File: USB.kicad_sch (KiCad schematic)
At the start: 10 parts, among them U401 ASDMB-26.000MHz-C, U402 USB3343

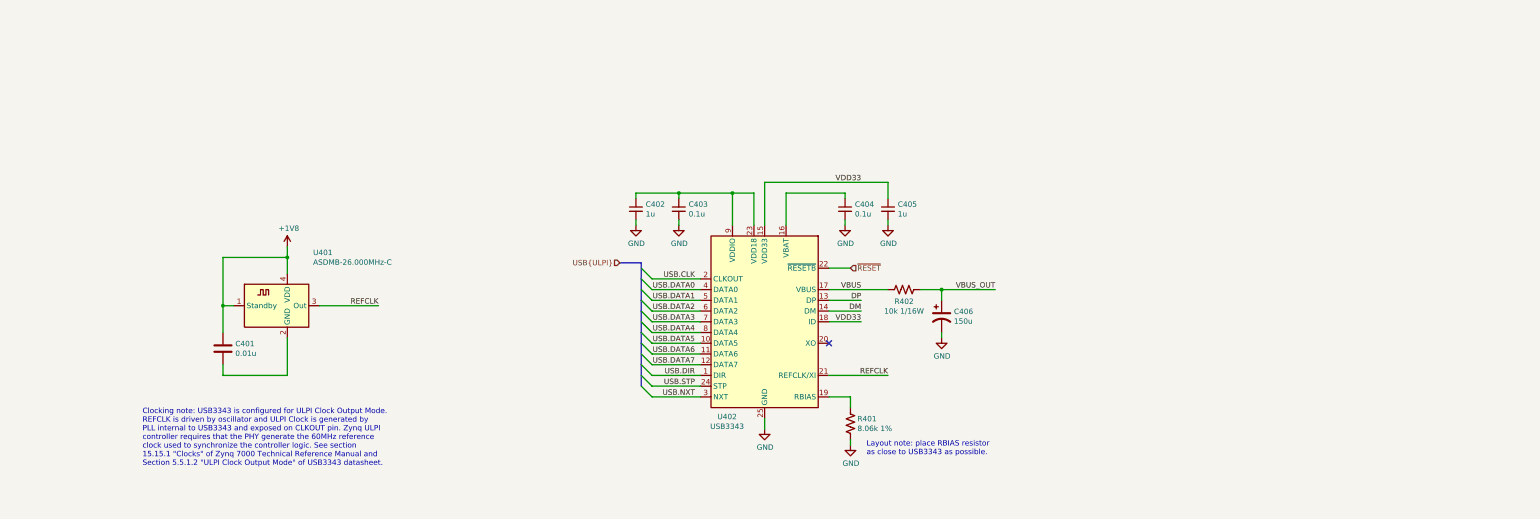
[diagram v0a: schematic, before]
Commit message: Fix footprint associations, use 74LVC2G07 instead of MOSFETs
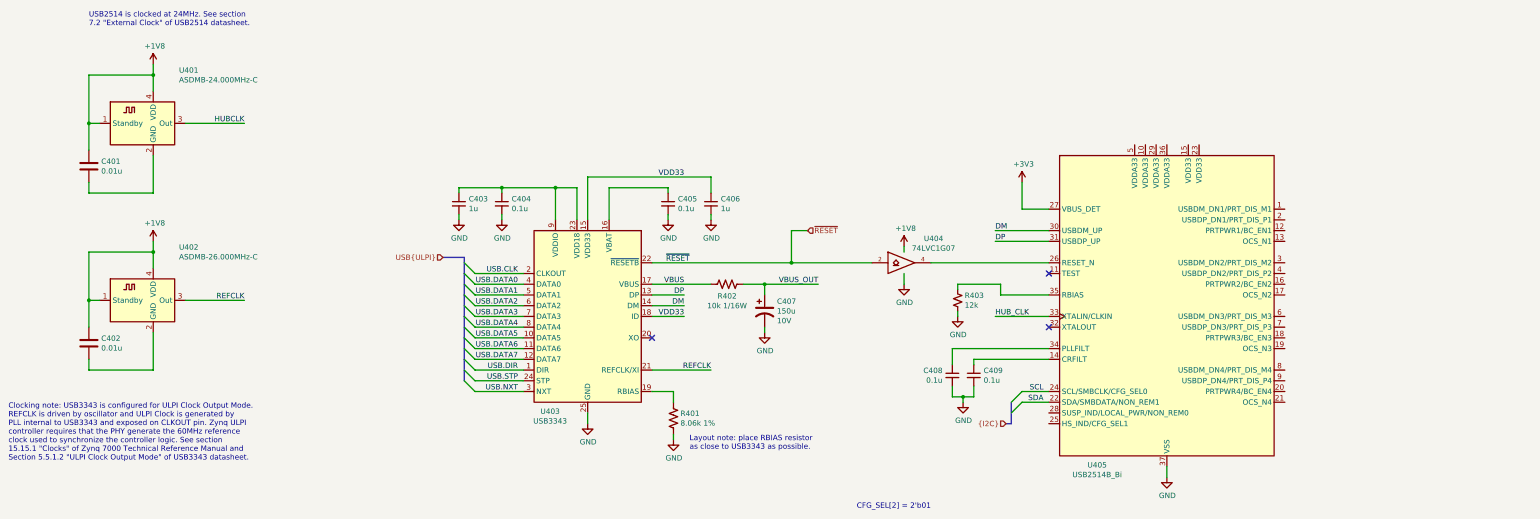
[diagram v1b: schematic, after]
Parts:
- added C401: 0.01u, Capacitor_SMD:C_0402_1005Metric, symbol Device:C
- added C408, C409: 0.1u, Capacitor_SMD:C_0402_1005Metric, symbol Device:C_Small
- added R403: 12k, Resistor_SMD:R_0402_1005Metric, symbol Device:R_Small_US
- added U401: ASDMB-24.000MHz-C, Oscillator:Oscillator_SMD_Abracon_ASDMB-4Pin_2.5x2.0mm, symbol Oscillator:ASDMB-xxxMHz
- added U404: 74LVC1G07, Package_TO_SOT_SMD:SOT-553, symbol 74xGxx:74LVC1G07
- added U405: USB2514B_Bi, Package_DFN_QFN:QFN-36-1EP_6x6mm_P0.5mm_EP3.7x3.7mm, symbol Interface_USB:USB2514B_Bi
- C402: renamed from C401; footprint (none) -> Capacitor_SMD:C_0402_1005Metric
- C403: renamed from C402; footprint (none) -> Capacitor_SMD:C_0402_1005Metric
- C404: renamed from C403; footprint (none) -> Capacitor_SMD:C_0402_1005Metric
- C405: renamed from C404; footprint (none) -> Capacitor_SMD:C_0402_1005Metric
- C406: renamed from C405; footprint (none) -> Capacitor_SMD:C_0402_1005Metric
- C407: renamed from C406; footprint (none) -> Capacitor_SMD:CP_Elec_3x5.3; Voltage (none) -> 10V
- R401, R402: footprint (none) -> Resistor_SMD:R_0402_1005Metric
- renumbered U401 to U402, U402 to U403
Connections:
- net +1V8: now also C401.1, U401.1 (Standby), U401.4 (VDD), U404.5 (VCC)
- net DM: now also U405.30 (USBDM_UP)
- net DP: now also U405.31 (USBDP_UP)
- net GND: now also C408.2, C409.2, R403.2, U404.3 (GND), U405.37 (VSS)
- net ~RESET: now also U404.2
- new net: C408.1, U405.34 (PLLFILT)
- new net: C409.1, U405.14 (CRFILT)
- new net: U404.4, U405.26 (RESET_N)
- new net: R403.1, U405.35 (RBIAS)
- new net: C401.2, U401.2 (GND)
- new net +3V3: U405.27 (VBUS_DET)
- new net HUBCLK: U401.3 (Out)
- new net HUB_CLK: U405.33 (XTALIN/CLKIN)
- new net SCL: U405.24 (SCL/SMBCLK/CFG_SEL0)
- new net SDA: U405.22 (SDA/SMBDATA/NON_REM1)
- no-connect marks 1 -> 3
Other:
- note added: "CFG_SEL[2] = 2'b01"
- note added: "USB2514 is clocked at 24MHz. See section 7.2 "External Clock" of USB2514 datasheet."
- moved on the sheet: C402, C403, C404, C405, C406, C407, R401, R402, U402, U403

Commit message: Connect Ethernet and USB to MIO, start layout
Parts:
- added J401, J402: USB_A, Connector_USB:USB_A_Molex_67643_Horizontal, symbol Connector:USB_A
- C401, C402, C403, C404, C405, C406, C408, C409: footprint Capacitor_SMD:C_0402_1005Metric -> Capacitor_SMD:C_0603_1608Metric
- R401, R402, R403: footprint Resistor_SMD:R_0402_1005Metric -> Resistor_SMD:R_0603_1608Metric
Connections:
- net D1P: now reaches U405.1 (USBDM_DN1/PRT_DIS_M1)
- net D1P: now also J401.3 (D+)
- net D1N: now reaches U405.2 (USBDP_DN1/PRT_DIS_P1)
- net D1N: now also J401.2 (D-)
- net D2P: now reaches U405.3 (USBDM_DN2/PRT_DIS_M2)
- net D2P: now also J402.3 (D+)
- net D2N: now reaches U405.4 (USBDP_DN2/PRT_DIS_P2)
- net D2N: now also J402.2 (D-)
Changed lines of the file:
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@@
   (junction (at 212.09 116.84) (diameter 0) (color 0 0 0 0))
   (junction (at 252.73 148.59) (diameter 0) (color 0 0 0 0))
+  (no_connect (at 273.05 119.38))
+  (no_connect (at 179.07 134.62))
   (no_connect (at 273.05 132.08))
-  (no_connect (at 179.07 134.62))
-  (no_connect (at 273.05 119.38))
   (bus_entry (at 134.62 116.84) (size 2.54 2.54)
     (stroke (width 0.1524) (type solid) (color 0 0 0 0))
@@
   )
   (wire (pts (xy 300.99 165.1) (xy 300.99 167.64))
+    (stroke (width 0) (type solid) (color 0 0 0 0))
+  )
+  (wire (pts (xy 328.93 104.14) (xy 341.63 104.14))
+    (stroke (width 0) (type solid) (color 0 0 0 0))
+  )
+  (wire (pts (xy 328.93 106.68) (xy 341.63 106.68))
+    (stroke (width 0) (type solid) (color 0 0 0 0))
+  )
+  (wire (pts (xy 328.93 116.84) (xy 341.63 116.84))
+    (stroke (width 0) (type solid) (color 0 0 0 0))
+  )
+  (wire (pts (xy 328.93 119.38) (xy 341.63 119.38))
+    (stroke (width 0) (type solid) (color 0 0 0 0))
+  )
+  (wire (pts (xy 377.19 88.9) (xy 386.08 88.9))
+    (stroke (width 0) (type solid) (color 0 0 0 0))
+  )
+  (wire (pts (xy 377.19 91.44) (xy 386.08 91.44))
+    (stroke (width 0) (type solid) (color 0 0 0 0))
+  )
+  (wire (pts (xy 378.46 129.54) (xy 387.35 129.54))
+    (stroke (width 0) (type solid) (color 0 0 0 0))
+  )
+  (wire (pts (xy 378.46 132.08) (xy 387.35 132.08))
     (stroke (width 0) (type solid) (color 0 0 0 0))
   )
@@
     (effects (font (size 1.27 1.27)) (justify right bottom))
   )
-  (hierarchical_label "USB{ULPI}" (shape input) (at 129.54 115.57 180)
+  (label "D1P" (at 341.63 104.14 180)
+    (effects (font (size 1.27 1.27)) (justify right bottom))
+  )
+  (label "D1N" (at 341.63 106.68 180)
+    (effects (font (size 1.27 1.27)) (justify right bottom))
+  )
+  (label "D2P" (at 341.63 116.84 180)
+    (effects (font (size 1.27 1.27)) (justify right bottom))
+  )
+  (label "D2N" (at 341.63 119.38 180)
+    (effects (font (size 1.27 1.27)) (justify right bottom))
+  )
+  (label "D1P" (at 386.08 88.9 180)
+    (effects (font (size 1.27 1.27)) (justify right bottom))
+  )
+  (label "D1N" (at 386.08 91.44 180)
+    (effects (font (size 1.27 1.27)) (justify right bottom))
+  )
+  (label "D2P" (at 387.35 129.54 180)
+    (effects (font (size 1.27 1.27)) (justify right bottom))
+  )
+  (label "D2N" (at 387.35 132.08 180)
+    (effects (font (size 1.27 1.27)) (justify right bottom))
+  )
+  (hierarchical_label "USB{ULPI}" (shape bidirectional) (at 129.54 115.57 180)
     (effects (font (size 1.27 1.27)) (justify right))
   )
@@
       (effects (font (size 1.27 1.27)) (justify left))
     )
-    (property "Footprint" "Resistor_SMD:R_0402_1005Metric" (id 2) (at 251.46 125.73 0)
+    (property "Footprint" "Resistor_SMD:R_0603_1608Metric" (id 2) (at 251.46 125.73 0)
       (effects (font (size 1.27 1.27)) hide)
     )
@@
       (effects (font (size 1.27 1.27)) (justify left))
     )
-    (property "Footprint" "Resistor_SMD:R_0402_1005Metric" (id 2) (at 185.166 153.924 90)
+    (property "Footprint" "Resistor_SMD:R_0603_1608Metric" (id 2) (at 185.166 153.924 90)
       (effects (font (size 1.27 1.27)) hide)
     )
@@
     (property "Reference" "R402" (id 0) (at 196.85 124.7204 90))
     (property "Value" "10k 1/16W" (id 1) (at 196.85 127.0191 90))
-    (property "Footprint" "Resistor_SMD:R_0402_1005Metric" (id 2) (at 197.104 120.904 90)
+    (property "Footprint" "Resistor_SMD:R_0603_1608Metric" (id 2) (at 197.104 120.904 90)
       (effects (font (size 1.27 1.27)) hide)
     )
@@
       (effects (font (size 1.27 1.27)) (justify left))
     )
-    (property "Footprint" "Capacitor_SMD:C_0402_1005Metric" (id 2) (at 133.35 102.87 0)
+    (property "Footprint" "Capacitor_SMD:C_0603_1608Metric" (id 2) (at 133.35 102.87 0)
       (effects (font (size 1.27 1.27)) hide)
     )
@@
       (effects (font (size 1.27 1.27)) (justify left))
     )
-    (property "Footprint" "Capacitor_SMD:C_0402_1005Metric" (id 2) (at 143.51 102.87 0)
+    (property "Footprint" "Capacitor_SMD:C_0603_1608Metric" (id 2) (at 143.51 102.87 0)
       (effects (font (size 1.27 1.27)) hide)
     )
@@
       (effects (font (size 1.27 1.27)) (justify left))
     )
-    (property "Footprint" "Capacitor_SMD:C_0402_1005Metric" (id 2) (at 182.88 102.87 0)
+    (property "Footprint" "Capacitor_SMD:C_0603_1608Metric" (id 2) (at 182.88 102.87 0)
       (effects (font (size 1.27 1.27)) hide)
     )
@@
       (effects (font (size 1.27 1.27)) (justify left))
     )
-    (property "Footprint" "Capacitor_SMD:C_0402_1005Metric" (id 2) (at 193.04 102.87 0)
+    (property "Footprint" "Capacitor_SMD:C_0603_1608Metric" (id 2) (at 193.04 102.87 0)
       (effects (font (size 1.27 1.27)) hide)
     )
@@
       (effects (font (size 1.27 1.27)) (justify right))
     )
-    (property "Footprint" "Capacitor_SMD:C_0402_1005Metric" (id 2) (at 250.19 143.51 0)
+    (property "Footprint" "Capacitor_SMD:C_0603_1608Metric" (id 2) (at 250.19 143.51 0)
       (effects (font (size 1.27 1.27)) hide)
     )
@@
       (effects (font (size 1.27 1.27)) (justify left))
     )
-    (property "Footprint" "Capacitor_SMD:C_0402_1005Metric" (id 2) (at 255.27 143.51 0)
+    (property "Footprint" "Capacitor_SMD:C_0603_1608Metric" (id 2) (at 255.27 143.51 0)
       (effects (font (size 1.27 1.27)) hide)
     )
@@
       (effects (font (size 1.27 1.27)) (justify left))
     )
-    (property "Footprint" "Capacitor_SMD:C_0402_1005Metric" (id 2) (at 46.6852 97.79 0)
+    (property "Footprint" "Capacitor_SMD:C_0603_1608Metric" (id 2) (at 46.6852 97.79 0)
       (effects (font (size 1.27 1.27)) hide)
     )
@@
       (effects (font (size 1.27 1.27)) (justify left))
     )
-    (property "Footprint" "Capacitor_SMD:C_0402_1005Metric" (id 2) (at 46.6852 139.7 0)
+    (property "Footprint" "Capacitor_SMD:C_0603_1608Metric" (id 2) (at 46.6852 139.7 0)
       (effects (font (size 1.27 1.27)) hide)
     )
@@
       (effects (font (size 1.27 1.27)) hide)
     )
+  )
+  (symbol (lib_id "Connector:USB_A") (at 369.57 88.9 0) (unit 1)
+    (in_bom yes) (on_board yes)
+    (property "Reference" "J401" (id 0) (at 370.967 77.0698 0))
+    (property "Value" "USB_A" (id 1) (at 370.967 79.3685 0))
+    (property "Footprint" "Connector_USB:USB_A_Molex_67643_Horizontal" (id 2) (at 373.38 90.17 0)
+      (effects (font (size 1.27 1.27)) hide)
+    )
+    (property "Datasheet" " ~" (id 3) (at 373.38 90.17 0)
+      (effects (font (size 1.27 1.27)) hide)
+    )
+  )
+  (symbol (lib_id "Connector:USB_A") (at 370.84 129.54 0) (unit 1)
+    (in_bom yes) (on_board yes)
+    (property "Reference" "J402" (id 0) (at 372.237 117.7098 0))
+    (property "Value" "USB_A" (id 1) (at 372.237 120.0085 0))
+    (property "Footprint" "Connector_USB:USB_A_Molex_67643_Horizontal" (id 2) (at 374.65 130.81 0)
+      (effects (font (size 1.27 1.27)) hide)
+    )
+    (property "Datasheet" " ~" (id 3) (at 374.65 130.81 0)
+      (effects (font (size 1.27 1.27)) hide)
+    )

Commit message: Place motor drivers, start layout of Ethernet PHY
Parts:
- C401, C402, C403, C404, C405, C406, C408, C409: footprint Capacitor_SMD:C_0603_1608Metric -> Capacitor_SMD:C_0402_1005Metric
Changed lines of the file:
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@@
-(kicad_sch (version 20200618) (host eeschema "5.99.0-unknown-77313e4~101~ubuntu20.04.1")
+(kicad_sch (version 20200618) (host eeschema "5.99.0-unknown-7340c97~102~ubuntu20.04.1")
   (page 4 14)
   (paper "B")
@@
   (junction (at 212.09 116.84) (diameter 0) (color 0 0 0 0))
   (junction (at 252.73 148.59) (diameter 0) (color 0 0 0 0))
+  (no_connect (at 179.07 134.62))
   (no_connect (at 273.05 119.38))
-  (no_connect (at 179.07 134.62))
   (no_connect (at 273.05 132.08))
   (bus_entry (at 134.62 116.84) (size 2.54 2.54)
@@
       (effects (font (size 1.27 1.27)) (justify left))
     )
-    (property "Footprint" "Capacitor_SMD:C_0603_1608Metric" (id 2) (at 133.35 102.87 0)
+    (property "Footprint" "Capacitor_SMD:C_0402_1005Metric" (id 2) (at 133.35 102.87 0)
       (effects (font (size 1.27 1.27)) hide)
     )
@@
       (effects (font (size 1.27 1.27)) (justify left))
     )
-    (property "Footprint" "Capacitor_SMD:C_0603_1608Metric" (id 2) (at 143.51 102.87 0)
+    (property "Footprint" "Capacitor_SMD:C_0402_1005Metric" (id 2) (at 143.51 102.87 0)
       (effects (font (size 1.27 1.27)) hide)
     )
@@
       (effects (font (size 1.27 1.27)) (justify left))
     )
-    (property "Footprint" "Capacitor_SMD:C_0603_1608Metric" (id 2) (at 182.88 102.87 0)
+    (property "Footprint" "Capacitor_SMD:C_0402_1005Metric" (id 2) (at 182.88 102.87 0)
       (effects (font (size 1.27 1.27)) hide)
     )
@@
       (effects (font (size 1.27 1.27)) (justify left))
     )
-    (property "Footprint" "Capacitor_SMD:C_0603_1608Metric" (id 2) (at 193.04 102.87 0)
+    (property "Footprint" "Capacitor_SMD:C_0402_1005Metric" (id 2) (at 193.04 102.87 0)
       (effects (font (size 1.27 1.27)) hide)
     )
@@
       (effects (font (size 1.27 1.27)) (justify right))
     )
-    (property "Footprint" "Capacitor_SMD:C_0603_1608Metric" (id 2) (at 250.19 143.51 0)
+    (property "Footprint" "Capacitor_SMD:C_0402_1005Metric" (id 2) (at 250.19 143.51 0)
       (effects (font (size 1.27 1.27)) hide)
     )
@@
       (effects (font (size 1.27 1.27)) (justify left))
     )
-    (property "Footprint" "Capacitor_SMD:C_0603_1608Metric" (id 2) (at 255.27 143.51 0)
+    (property "Footprint" "Capacitor_SMD:C_0402_1005Metric" (id 2) (at 255.27 143.51 0)
       (effects (font (size 1.27 1.27)) hide)
     )
@@
       (effects (font (size 1.27 1.27)) (justify left))
     )
-    (property "Footprint" "Capacitor_SMD:C_0603_1608Metric" (id 2) (at 46.6852 97.79 0)
+    (property "Footprint" "Capacitor_SMD:C_0402_1005Metric" (id 2) (at 46.6852 97.79 0)
       (effects (font (size 1.27 1.27)) hide)
     )
@@
       (effects (font (size 1.27 1.27)) (justify left))
     )
-    (property "Footprint" "Capacitor_SMD:C_0603_1608Metric" (id 2) (at 46.6852 139.7 0)
-      (effects (font (size 1.27 1.27)) hide)
-    )
+    (property "Footprint" "Capacitor_SMD:C_0402_1005Metric" (id 2) (at 46.6852 139.7 0)
+      (effects (font (size 1.27 1.27)) hide)
+    )

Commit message: Add FTDI chip
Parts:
- renumbered C401 to C501, C402 to C502, C403 to C503, C404 to C504, C405 to C505, C406 to C506, C407 to C507, C408 to C508, C409 to C509, J401 to J501, J402 to J502, R401 to R501, R402 to R502, R403 to R503, U401 to U501, U402 to U502, U403 to U503, U404 to U504, U405 to U505

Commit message: Attach ethernet to PL, layout and route
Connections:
- net ~HUB_RESET: now reaches U504.4, U505.26 (RESET_N)
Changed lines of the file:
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@@
-(kicad_sch (version 20200714) (host eeschema "5.99.0-unknown-bf445c1~102~ubuntu20.04.1")
-  (page 1 15)
+(kicad_sch (version 20200714) (host eeschema "5.99.0-unknown-a146cd9~102~ubuntu20.04.1")
+  (page 5 15)
   (paper "B")
   (title_block
@@
   )
   (bus_alias "ULPI" (members "DATA[7..0]" "CLK" "STP" "DIR" "NXT"))
-  (junction (at 45.72 83.82) (diameter 0) (color 0 0 0 0))
-  (junction (at 45.72 125.73) (diameter 0) (color 0 0 0 0))
-  (junction (at 60.96 72.39) (diameter 0) (color 0 0 0 0))
-  (junction (at 60.96 114.3) (diameter 0) (color 0 0 0 0))
-  (junction (at 143.51 99.06) (diameter 0) (color 0 0 0 0))
-  (junction (at 156.21 99.06) (diameter 0) (color 0 0 0 0))
-  (junction (at 205.74 121.92) (diameter 0) (color 0 0 0 0))
-  (junction (at 212.09 116.84) (diameter 0) (color 0 0 0 0))
-  (junction (at 252.73 148.59) (diameter 0) (color 0 0 0 0))
-  (no_connect (at 273.05 132.08))
+  (junction (at 45.72 83.82) (diameter 1.016) (color 0 0 0 0))
+  (junction (at 45.72 125.73) (diameter 1.016) (color 0 0 0 0))
+  (junction (at 60.96 72.39) (diameter 1.016) (color 0 0 0 0))
+  (junction (at 60.96 114.3) (diameter 1.016) (color 0 0 0 0))
+  (junction (at 143.51 99.06) (diameter 1.016) (color 0 0 0 0))
+  (junction (at 156.21 99.06) (diameter 1.016) (color 0 0 0 0))
+  (junction (at 205.74 121.92) (diameter 1.016) (color 0 0 0 0))
+  (junction (at 212.09 116.84) (diameter 1.016) (color 0 0 0 0))
+  (junction (at 252.73 148.59) (diameter 1.016) (color 0 0 0 0))
   (no_connect (at 179.07 134.62))
   (no_connect (at 273.05 119.38))
+  (no_connect (at 273.05 132.08))
   (bus_entry (at 134.62 116.84) (size 2.54 2.54)
     (stroke (width 0.1524) (type solid) (color 0 0 0 0))
@@
     (stroke (width 0) (type solid) (color 0 0 0 0))
   )
-  (bus (pts (xy 134.62 119.38) (xy 134.62 124.46))
-    (stroke (width 0) (type solid) (color 0 0 0 0))
-  )
-  (bus (pts (xy 134.62 124.46) (xy 134.62 129.54))
-    (stroke (width 0) (type solid) (color 0 0 0 0))
-  )
-  (bus (pts (xy 134.62 129.54) (xy 134.62 134.62))
-    (stroke (width 0) (type solid) (color 0 0 0 0))
-  )
-  (bus (pts (xy 134.62 134.62) (xy 134.62 139.7))
-    (stroke (width 0) (type solid) (color 0 0 0 0))
-  )
-  (bus (pts (xy 134.62 139.7) (xy 134.62 144.78))
+  (bus (pts (xy 134.62 119.38) (xy 134.62 121.92))
+    (stroke (width 0) (type solid) (color 0 0 0 0))
+  )
+  (bus (pts (xy 134.62 121.92) (xy 134.62 127))
+    (stroke (width 0) (type solid) (color 0 0 0 0))
+  )
+  (bus (pts (xy 134.62 127) (xy 134.62 132.08))
+    (stroke (width 0) (type solid) (color 0 0 0 0))
+  )
+  (bus (pts (xy 134.62 132.08) (xy 134.62 137.16))
+    (stroke (width 0) (type solid) (color 0 0 0 0))
+  )
+  (bus (pts (xy 134.62 137.16) (xy 134.62 142.24))
+    (stroke (width 0) (type solid) (color 0 0 0 0))
+  )
+  (bus (pts (xy 134.62 142.24) (xy 134.62 144.78))
     (stroke (width 0) (type solid) (color 0 0 0 0))
   )
@@
     (effects (font (size 1.27 1.27)) (justify right bottom))
   )
-  (label "~RESET" (at 187.96 116.84 180)
+  (label "~ULPI_RESET" (at 193.04 116.84 180)
     (effects (font (size 1.27 1.27)) (justify right bottom))
   )
@@
     (effects (font (size 1.27 1.27)) (justify left bottom))
   )
+  (label "~HUB_RESET" (at 260.35 116.84 0)
+    (effects (font (size 1.27 1.27)) (justify left bottom))
+  )
